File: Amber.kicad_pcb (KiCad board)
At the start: 4 copper layers, 120 x 120 mm, 308 parts, among them J1 Barrel_Jack, J10 Conn_02x04_Odd_Even, J11 Conn_02x05_Odd_Even, J12 Bus_M.2_Socket_M, J13 Conn_01x03_Male, J2 RJ45_LINK-PP_LPJG0926HENL_Hor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, J3 USB_C_Receptacle_USB2.0, J4 USB_A_Stacked, J5 AudioJack, J6 HDMI_D_2.0, J7 Micro_SD_Card_Det, J8 SiLabs Mini Debug, J9 Conn_Coaxial, M1 Fan_4pin, Q1 DMP3013SFV-7, Q2 BSZ440N10NS3GATMA1, SW1 SW_USER, SW2 SW_WIPE, T1 PA2467NL, U1 RaspberryPi-CM4Lite, U10 TPD4EUSB30, U11 SiliconLabs-MGM210P, U12 PCM5121PW, U13 TLV74033PDBVR, U14 TPD4EUSB30, U15 TPD4EUSB30, U16 BD9D321EFJ, U17 BD9D321EFJ, U18 74LVC1G07, U19 74LVC1G07, U2 DF40C-100DS-0.4V, U20 LP5569RTWR, U21 PCF85063AT, U22 RT9742GGJ5, U23 TPS23734, U24 TCMT1107, U3 DF40C-100DS-0.4V, U4 CP2102N-Axx-xQFN20, U5 FSUSB42MUX, U6 FSUSB42MUX, U7 USB2422, U8 TPD4EUSB30, U9 AP2191W, Y1 24MHz, Y2 X32K768S301

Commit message: Renmae LightBlue to Amber
Signed-off-by: Stefan Agner <stefan@agner.ch>
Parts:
- H5, H6: footprint LightBlue:DrillSlot_Plated_3.5x2.5mm -> Amber:DrillSlot_Plated_3.5x2.5mm
- HS1: footprint LightBlue:Heatsink_56x56mm_2xFixation3.2mm -> Amber:Heatsink_56x56mm_2xFixation3.2mm
- J1: footprint LightBlue:BarrelJack_CUI_PJ-002A -> Amber:BarrelJack_CUI_PJ-002A
- J12: footprint LightBlue:TE_1-2199230-3_Bus_M.2_M_H4.2mm_P0.5mm_2280_Horizontal -> Amber:TE_1-2199230-3_Bus_M.2_M_H4.2mm_P0.5mm_2280_Horizontal
- J2: footprint LightBlue:RJ45_LINK-PP_LPJG0926HENL_Horizontal -> Amber:RJ45_LINK-PP_LPJG0926HENL_Horizontal
- J5: footprint LightBlue:Jack_3.5mm_HRO_PJ-3973-6A_Horizontal -> Amber:Jack_3.5mm_HRO_PJ-3973-6A_Horizontal
- Q2: footprint LightBlue:PG-TSDSON-8 -> Amber:PG-TSDSON-8
- REF** (x14): footprint LightBlue:DrillSlot_Plated_5x3mm -> Amber:DrillSlot_Plated_5x3mm
- Ref**: footprint LightBlue:SilkScreen_UART-USB-Mux -> Amber:SilkScreen_UART-USB-Mux
- Ref**: footprint LightBlue:Logo_HomeAssitant_Inverted -> Amber:Logo_HomeAssitant_Inverted
- Ref**: footprint LightBlue:Logo_NabuCasa -> Amber:Logo_NabuCasa
- Ref**: footprint LightBlue:SilkScreen_USB-Boot -> Amber:SilkScreen_USB-Boot
- Ref**: footprint LightBlue:SilkScreen_PoE-Text -> Amber:SilkScreen_PoE-Text
- Ref**: footprint LightBlue:SilkScreen_Radio-Text -> Amber:SilkScreen_Radio-Text
- Ref**: footprint LightBlue:SilkScreen_CM4-Text -> Amber:SilkScreen_CM4-Text
- Ref**: footprint LightBlue:SilkScreen_Class-Selection -> Amber:SilkScreen_Class-Selection
- Ref**: footprint LightBlue:SilkScreen_M.2-Text -> Amber:SilkScreen_M.2-Text
- T1: footprint LightBlue:Transformer_Pulse_PA2467NL -> Amber:Transformer_Pulse_PA2467NL
- U1: footprint LightBlue:RaspberryPi-CM4 -> Amber:RaspberryPi-CM4
- U11: footprint LightBlue:SiliconLabs_MGM210P -> Amber:SiliconLabs_MGM210P
- U2, U3: footprint LightBlue:Hirose_DF40_DF40C-100DS-0.4V_2x50_P0.40mm_Vertical_Virtual -> Amber:Hirose_DF40_DF40C-100DS-0.4V_2x50_P0.40mm_Vertical_Virtual
- U23: footprint LightBlue:Texas_VQFN-47-2EP_5x7mm_P0.4mm_ThermalVias -> Amber:Texas_VQFN-47-2EP_5x7mm_P0.4mm_ThermalVias

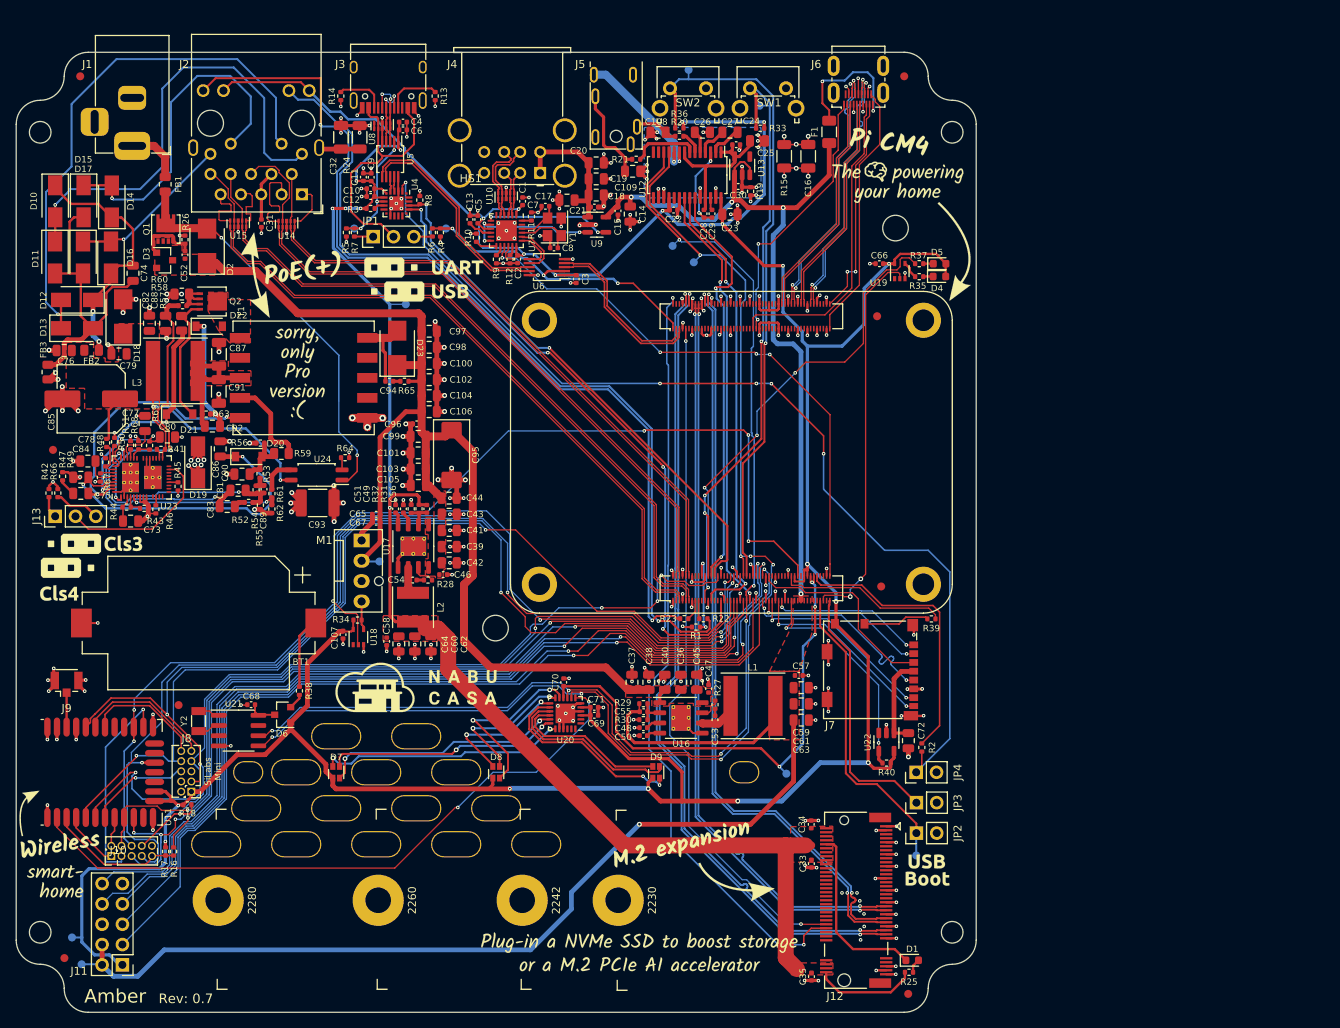
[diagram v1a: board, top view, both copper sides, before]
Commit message: Relayout new design
- Update PCB from Schematics
- Move SD-card to bottom side of the PCB
- Place LEDs in front of CM4
- Add additional LEDs (Amber/Radio)
- Move LP5569 to the left
- Remove all holes
- Lock through holes which should not be moved

Fixes: #33

Signed-off-by: Stefan Agner <stefan@agner.ch>
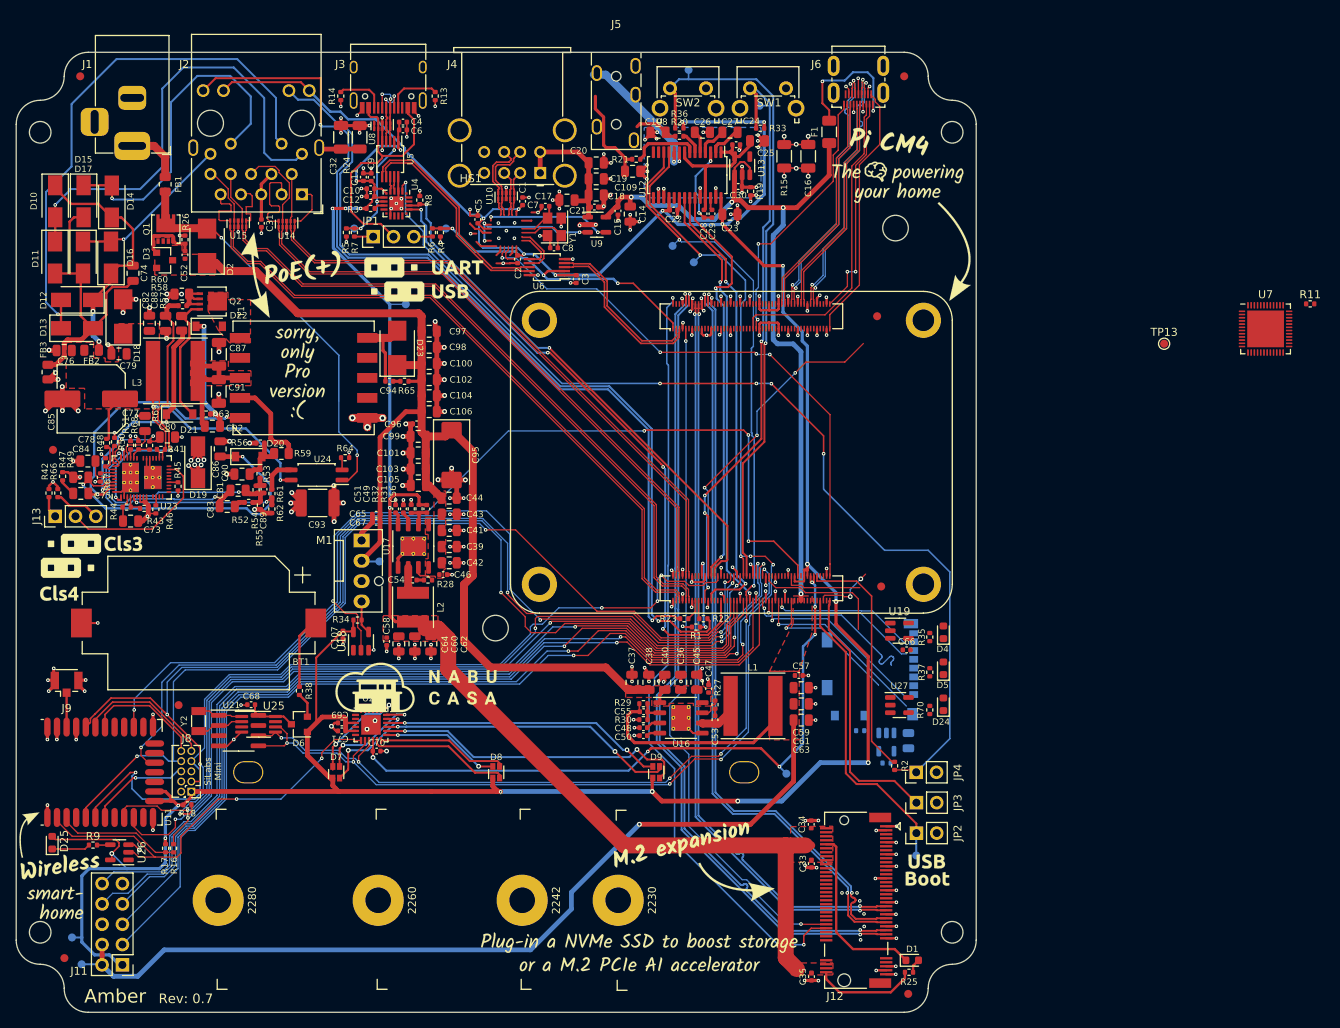
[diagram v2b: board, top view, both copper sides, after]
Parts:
- removed C13: 1u, Capacitor_SMD:C_0402_1005Metric
- removed J10: Conn_02x04_Odd_Even, Connector_PinHeader_1.27mm:PinHeader_2x05_P1.27mm_Vertical
- removed R10, R12: 10k, Resistor_SMD:R_0402_1005Metric
- removed REF** (x14): DrillSlot_Plated_5x3mm, Amber:DrillSlot_Plated_5x3mm
- added D24: LED Yellow, LED_SMD:LED_0603_1608Metric, F.Cu at (145.9, 111.5)
- added D25: LED Blue, LED_SMD:LED_0603_1608Metric, F.Cu at (34.5, 128.8)
- added R70: 1k, Resistor_SMD:R_0402_1005Metric, F.Cu at (144.2, 112.2)
- added TP13: TestPoint, TestPoint:TestPoint_Pad_D1.0mm, F.Cu at (173.5, 66.4)
- added U25: PCF8563TS, Package_SO:MSOP-8_3x3mm_P0.65mm, F.Cu at (60.3, 114.0)
- added U26: 74LVC1G07, Package_TO_SOT_SMD:SOT-23-5, F.Cu at (42.9, 130.0)
- added U27: 74LVC1G07, Package_TO_SOT_SMD:SOT-23-5, F.Cu at (140.4, 111.6)
- C5: value 1u -> 10u
- C7, C8: value 18p -> 10p
- C72, J7, R39, R40, U22: moved to B.Cu
- J5: footprint Amber:Jack_3.5mm_HRO_PJ-3973-6A_Horizontal -> Amber:Jack_3.5mm_XKB_PJ-3270_Horizontal
- R11: value 12k/1% -> 2.7k/1%
- R9: value 10k -> 1k
- U18, U19: footprint Package_TO_SOT_SMD:SOT-353_SC-70-5 -> Package_TO_SOT_SMD:SOT-23-5
- U7: value USB2422 -> FE1.1; footprint Package_DFN_QFN:QFN-24-1EP_4x4mm_P0.5mm_EP2.6x2.6mm -> Package_DFN_QFN:QFN-48-1EP_6x6mm_P0.4mm_EP4.6x4.6mm
- Y1: value 24MHz -> 12MHz
- moved R11 98.0 mm to (191.8, 61.5), turned to 0 degrees
- moved U7 95.7 mm to (186.2, 64.6), turned to 0 degrees
- moved R9 88.9 mm to (39.6, 129.1), turned to 0 degrees
- moved R37 51.1 mm to (144.2, 107.5), turned to 90 degrees
- moved D5 50.6 mm to (145.9, 107.0), turned to 90 degrees
- moved C66 48.4 mm to (141.3, 104.7)
- moved R35 45.1 mm to (144.2, 103.1), turned to 90 degrees
- moved U19 45.0 mm to (140.4, 102.3), turned to 0 degrees
- moved D4 44.5 mm to (145.9, 102.5), turned to 90 degrees
- moved C71 31.7 mm to (70.7, 114.8), turned to 180 degrees
- moved C69 31.6 mm to (70.7, 113.8), turned to 180 degrees
- moved C70 24.9 mm to (75.0, 117.3), turned to 0 degrees
- moved U20 24.3 mm to (74.3, 114.1), turned to 0 degrees
- moved R39 16.6 mm to (135.5, 114.8), turned to 180 degrees
- moved R2 4.10 mm to (139.8, 119.2)
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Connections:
- net /802.15.4 Radio/Radio.~BOOT renamed /802.15.4 Radio/Radio.~{BOOT}
- net /802.15.4 Radio/Radio.~RESET renamed /802.15.4 Radio/Radio.~{RESET}
- net /802.15.4 Radio/~LED_RADIO renamed /802.15.4 Radio/~{LED_RADIO}
- net /CM4/PCIe.~CLKREQ renamed /CM4/PCIe.~{CLKREQ}
- net /CM4/PCIe.~RST renamed /CM4/PCIe.~{RST}
- net /CM4/~FAN_PWM renamed /CM4/~{FAN_PWM}
- net /CM4/~LED_ACT renamed /CM4/~{LED_ACT}
- net /CM4/~LED_PWR renamed /CM4/~{LED_PWR}
- net /CM4/~RPI_BOOT renamed /CM4/~{RPI_BOOT}
- net /CM4/~SW_USER renamed /CM4/~{SW_USER}
- net /CM4/~SW_WIPE renamed /CM4/~{SW_WIPE}
- net /PoE/DC_IN_F renamed /Power/DC_IN_F
- C76 pad 2: VSS -> GND
- C79 pad 2: VSS -> GND
- D18 pad 2: VSS -> GND
- D19 pad 2: VSS -> GND
- FB3 pad 2: VSS -> GND
- J5 pad R2: unconnected-(J5-PadR2) -> GNDA
- R42 pad 1: VSS -> GND
- R45 pad 1: VSS -> GND
- R66 pad 1: VSS -> GND
- R9 pad 1: GND -> Net-(D25-Pad1)
- U1 pad 100: /CM4/~EXTRST -> /CM4/~{EXTRST}
- U1 pad 82: unconnected-(U1-Pad82) -> /CM4/~{LED_AMBER}
- U23 pad 27: VSS -> GND
- U23 pad 28: VSS -> GND
- U23 pad 47: VSS -> GND
- U7 pad 1: +3V3 -> GND
- U7 pad 10: Net-(C13-Pad1) -> GND
- U7 pad 11: unconnected-(U7-Pad11) -> Net-(C7-Pad1)
- U7 pad 12: /USB/~USB_OC -> Net-(C8-Pad1)
- U7 pad 13: Net-(R10-Pad2) -> +3V3
- U7 pad 14: Net-(R9-Pad2) -> unconnected-(U7-Pad14)
- U7 pad 15: /CM4/~EXTRST -> unconnected-(U7-Pad15)
- U7 pad 16: +3V3 -> GND
- U7 pad 17: Net-(R12-Pad2) -> unconnected-(U7-Pad17)
- U7 pad 18: +3V3 -> unconnected-(U7-Pad18)
- U7 pad 19: /USB/HUB.D- -> +3V3
- U7 pad 2: /USB/USB0.D- -> unconnected-(U7-Pad2)
- U7 pad 20: /USB/HUB.D+ -> /USB/USB1.D-
- U7 pad 21: Net-(C8-Pad1) -> /USB/USB1.D+
- U7 pad 22: Net-(C7-Pad1) -> GND
- U7 pad 23: unconnected-(U7-Pad23) -> /USB/USB0.D-
- U7 pad 24: Net-(R11-Pad2) -> /USB/USB0.D+
- U7 pad 3: /USB/USB0.D+ -> VD18
- U7 pad 4: /USB/USB1.D- -> unconnected-(U7-Pad4)
- U7 pad 5: /USB/USB1.D+ -> GND
- U7 pad 6: (no net) -> GND
- U7 pad 7: /USB/USB_PWR_EN -> GND
- U7 pad 8: /USB/~USB_OC -> GND
- U7 pad 9: +3V3 -> VD18
- U9 pad 3: /USB/~USB_OC -> /USB/~{USB_OC}
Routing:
- net /CM4/~{EXTRST}: track 0.00 -> 70.8 mm, vias 0 -> 4
- net /CM4/~EXTRST: track 70.8 -> 0.00 mm, vias 4 -> 0
- net +3V3: track 448.5 -> 397.0 mm
- net /CM4/~{LED_PWR}: track 48.6 -> 7.62 mm
- net /802.15.4 Radio/~{LED_RADIO}: track 81.6 -> 51.7 mm
- net /802.15.4 Radio/PC00: track 25.9 -> 0.00 mm, vias 1 -> 0
- net +1V8: track 63.1 -> 84.1 mm, vias 4 -> 6
- net /802.15.4 Radio/Radio.RTS: track 133.8 -> 113.7 mm
- net VSS: track 19.7 -> 0.00 mm, vias 11 -> 0
- net Net-(D7-Pad1): track 31.0 -> 13.2 mm
- net /USB/~{USB_OC}: track 0.00 -> 17.3 mm, vias 0 -> 3
- net /USB/~USB_OC: track 17.3 -> 0.00 mm, vias 3 -> 0
- net Net-(D7-Pad3): track 30.4 -> 13.2 mm
- net Net-(D9-Pad1): track 19.8 -> 35.5 mm, vias 0 -> 2
- net /802.15.4 Radio/Radio.CTS: track 127.8 -> 112.1 mm, vias 5 -> 4
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- removed copper zone on In2.Cu, net VSS

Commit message: [WIP] PCB design
Done:
PoE - primary side,
DCDC location,
USB hub location,

TBD:
HUB routing,
PoE sec. side,
Audio

Signed-off-by: Dominik Sliwa <dominik@sliwa.io>
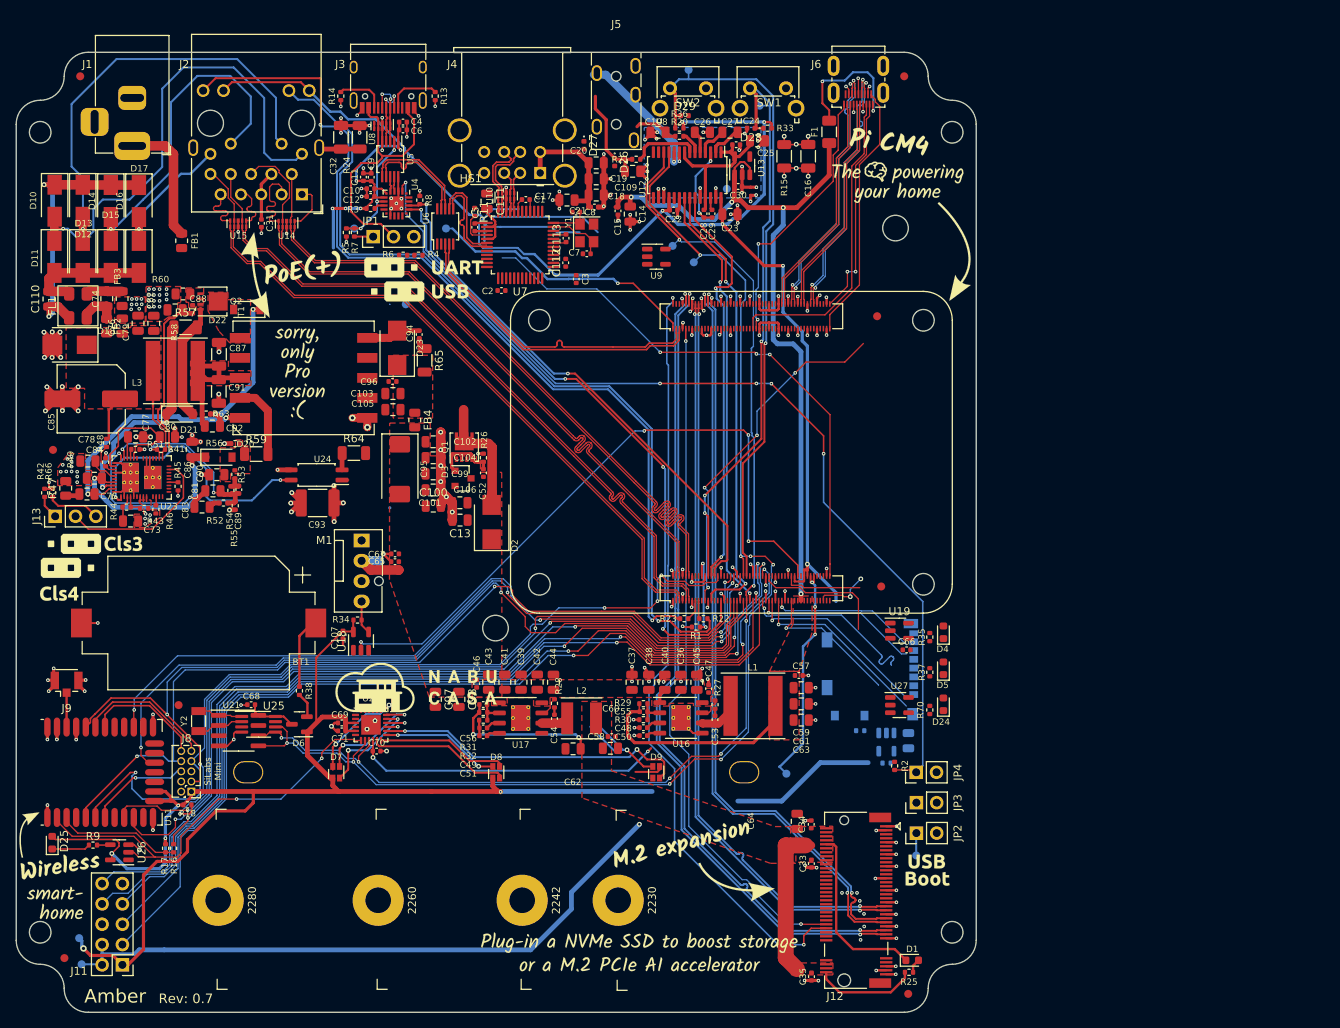
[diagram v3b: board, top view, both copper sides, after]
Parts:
- removed D19: B1100-13-F, Diode_SMD:D_SMA
- removed R19, R50, R67, R68, R69: 0R, Resistor_SMD:R_0402_1005Metric
- removed R61, R62: 22k, Resistor_SMD:R_0402_1005Metric
- added C110: 1n/100V, Capacitor_SMD:C_0805_2012Metric, F.Cu at (34.1, 60.8)
- added C111: 10u, Capacitor_SMD:C_0805_2012Metric, F.Cu at (88.8, 48.6)
- added C112: 100n, Capacitor_SMD:C_0402_1005Metric, F.Cu at (98.7, 56.3)
- added C113: 100n, Capacitor_SMD:C_0402_1005Metric, F.Cu at (98.7, 53.2)
- added C13: 22u/25V, Capacitor_SMD:C_0805_2012Metric, F.Cu at (85.5, 88.5)
- added D26: D_TVS, Diode_SMD:D_0402_1005Metric, F.Cu at (104.8, 43.7)
- added D27: D_TVS, Diode_SMD:D_0402_1005Metric, F.Cu at (101.0, 41.6)
- added D28: D_TVS, Diode_SMD:D_0402_1005Metric, F.Cu at (121.8, 39.5)
- added D29: D_TVS, Diode_SMD:D_0402_1005Metric, F.Cu at (113.5, 37.9)
- added FB4: 300R/3A, Resistor_SMD:R_0805_2012Metric, F.Cu at (79.8, 76.0)
- added FL1: 1k@100MHz/500mA, Amber:Murata_DLW5B, F.Cu at (37.7, 61.7)
- JP1: value JP_USB_DEVICE_SEL -> Conn_01x03_Male
- R47: footprint Resistor_SMD:R_0402_1005Metric -> Resistor_SMD:R_0805_2012Metric
- R57: footprint Resistor_SMD:R_0805_2012Metric -> Resistor_SMD:R_1206_3216Metric
- R59: value 3R9/1% -> 3R0/1%; footprint Resistor_SMD:R_0805_2012Metric -> Resistor_SMD:R_1206_3216Metric
- R64: value 22k -> 1k2; footprint Resistor_SMD:R_0402_1005Metric -> Resistor_SMD:R_1206_3216Metric
- R65: value 5R1 -> 4R7; footprint Resistor_SMD:R_0402_1005Metric -> Resistor_SMD:R_1206_3216Metric
- TP13: moved to B.Cu
- U7: footprint Package_DFN_QFN:QFN-48-1EP_6x6mm_P0.4mm_EP4.6x4.6mm -> Package_QFP:TQFP-48_7x7mm_P0.5mm
- Y1: value 12MHz -> 12MHz/10pF
- Y2: value X32K768S301 -> 32768Hz/12.5pF
- moved R11 105.1 mm to (87.3, 50.0), turned to -90 degrees
- moved U7 93.8 mm to (93.0, 54.1), turned to 180 degrees
- moved TP13 58.0 mm to (118.8, 47.1), turned to 180 degrees
- moved C64 54.5 mm to (127.6, 126.1), turned to 90 degrees
- moved D2 49.6 mm to (89.4, 88.7)
- moved D3 46.2 mm to (85.9, 83.3)
- moved R26 46.2 mm to (88.4, 80.7)
- moved C52 46.2 mm to (88.4, 82.6)
- moved Q1 46.2 mm to (86.0, 79.4)
- moved C97 46.0 mm to (82.4, 110.9), turned to -90 degrees
- moved C98 44.2 mm to (85.3, 110.9), turned to -90 degrees
- moved C58 30.5 mm to (104.4, 115.5), turned to 0 degrees
- moved C51 30.4 mm to (88.4, 115.4), turned to 180 degrees
- moved C49 29.2 mm to (88.4, 114.5), turned to 180 degrees
- moved R32 27.9 mm to (88.4, 113.5), turned to 0 degrees
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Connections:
- C103 pad 1: +12V -> Net-(C103-Pad1)
- C105 pad 1: +12V -> Net-(C103-Pad1)
- C108 pad 1: GNDA -> GND
- C109 pad 2: GNDA -> GND
- C24 pad 2: GNDA -> GND
- C25 pad 2: GNDA -> GND
- C26 pad 2: GNDA -> GND
- C28 pad 2: GNDA -> GND
- C29 pad 1: GNDA -> GND
- C30 pad 2: GNDA -> GND
- C76 pad 2: GND -> GNDS
- C79 pad 2: GND -> GNDS
- C96 pad 1: +12V -> Net-(C103-Pad1)
- D10 pad 1: Net-(C74-Pad1) -> Net-(C110-Pad1)
- D11 pad 2: Net-(C74-Pad2) -> Net-(C110-Pad2)
- D12 pad 1: Net-(C74-Pad1) -> Net-(C110-Pad1)
- D13 pad 2: Net-(C74-Pad2) -> Net-(C110-Pad2)
- D14 pad 1: Net-(C74-Pad1) -> Net-(C110-Pad1)
- D15 pad 2: Net-(C74-Pad2) -> Net-(C110-Pad2)
- D16 pad 1: Net-(C74-Pad1) -> Net-(C110-Pad1)
- D17 pad 2: Net-(C74-Pad2) -> Net-(C110-Pad2)
- D18 pad 2: GND -> GNDS
- D23 pad 1: +12V -> Net-(C103-Pad1)
- FB3 pad 2: GND -> GNDS
- J5 pad R2: GNDA -> GND
- J5 pad S: GNDA -> GND
- R41 pad 2: Net-(R41-Pad2) -> /PoE/DEN
- R42 pad 1: GND -> GNDS
- R45 pad 1: GND -> GNDS
- R65 pad 2: +12V -> Net-(C103-Pad1)
- R66 pad 1: GND -> GNDS
- U11 pad 21: /802.15.4 Radio/PC00 -> unconnected-(U11-Pad21)
- U11 pad 4: /802.15.4 Radio/PA00 -> unconnected-(U11-Pad4)
- U11 pad 8: /802.15.4 Radio/PA04 -> unconnected-(U11-Pad8)
- U12 pad 10: GNDA -> GND
- U12 pad 3: GNDA -> GND
- U12 pad 9: GNDA -> GND
- U13 pad 2: GNDA -> GND
- U23 pad 24: Net-(R41-Pad2) -> /PoE/DEN
- U23 pad 27: GND -> GNDS
- U23 pad 28: GND -> GNDS
- U23 pad 31: Net-(R68-Pad1) -> /PoE/VB
- U23 pad 36: Net-(R50-Pad1) -> GND1
- U23 pad 39: Net-(R67-Pad1) -> GND1
- U23 pad 47: GND -> GNDS
- U23 pad 5: /PoE/APD -> GND1
- U24 pad 3: Net-(R61-Pad1) -> GNDS
- U24 pad 4: +48V -> /PoE/DEN
- U7 pad 20: /USB/USB1.D- -> /USB/USB0.D-
- U7 pad 21: /USB/USB1.D+ -> /USB/USB0.D+
- U7 pad 23: /USB/USB0.D- -> /USB/USB1.D-
- U7 pad 24: /USB/USB0.D+ -> /USB/USB1.D+
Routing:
- net +12V: track 142.5 -> 9.25 mm
- net +3.3VP: track 181.9 -> 81.2 mm, vias 6 -> 7
- net GNDA: track 45.5 -> 0.00 mm, vias 18 -> 0
- net /CM4/~{RPI_BOOT}: track 38.3 -> 2.81 mm
- net Net-(C110-Pad1): track 0.00 -> 33.6 mm, vias 0 -> 2
- net +5V: track 235.2 -> 202.5 mm
- net Net-(C74-Pad2): track 37.1 -> 4.58 mm
- net /CM4/GLOBAL_EN: track 32.5 -> 0.00 mm
- net Net-(D9-Pad2): track 37.0 -> 5.00 mm, vias 2 -> 1
- net /CM4/RUN_PG: track 30.3 -> 0.00 mm
- net /Power/DC_IN_F: track 50.7 -> 20.6 mm, vias 2 -> 0
- net Net-(C74-Pad1): track 31.9 -> 4.98 mm, vias 2 -> 0
- net /PoE/DEN: track 0.00 -> 25.7 mm, vias 0 -> 2
- net +3V3: track 397.0 -> 372.4 mm, vias 18 -> 11
- net Net-(D9-Pad1): track 35.5 -> 11.6 mm
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- added copper zone on F.Cu, net /PoE/V_{REG}
- added copper zone on B.Cu, net GND
- added copper zone on F.Cu, net GND1
- added copper zone on F.Cu, net GNDS
- added copper zone on In2.Cu, net GNDS
- added copper zone on F.Cu, net Net-(C103-Pad1)
- added copper zone on F.Cu, net Net-(Q2-Pad1)
- removed copper zone on B.Cu, net GNDA
